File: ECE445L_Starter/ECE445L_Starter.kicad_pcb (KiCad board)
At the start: 2 copper layers, 115 x 94 mm, 20 parts, among them J101 EXT_3V3, Q101 IRLD024PBF, SW101 UP, SW102 DOWN, SW103 LEFT, SW104 RIGHT, SW105 MODE, U101 EK-TM4C123GXL, U102 ESP8266-1, U103 Adafruit ST7735R

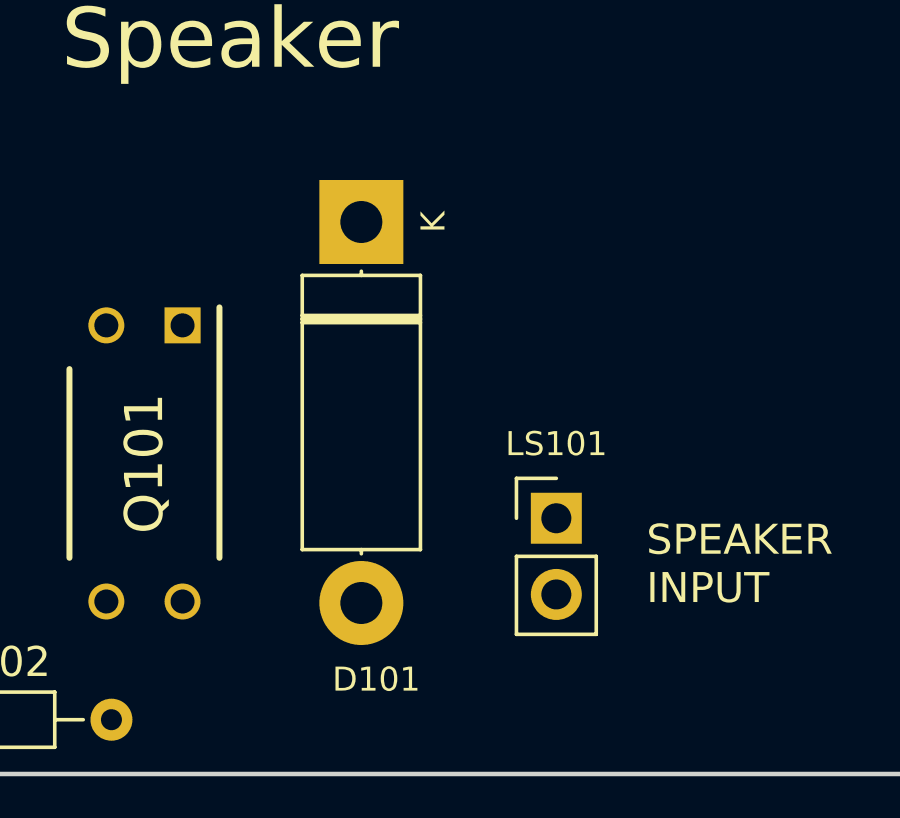
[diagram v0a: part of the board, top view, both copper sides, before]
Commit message: update all symbols and re-sync footprints in the KiCad projects
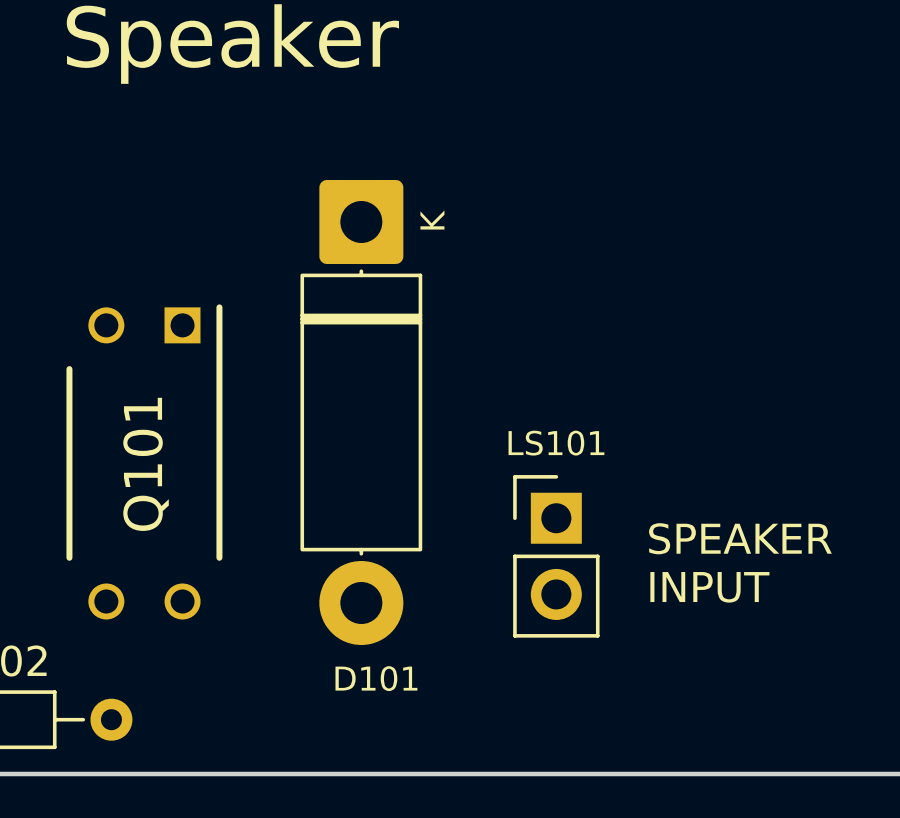
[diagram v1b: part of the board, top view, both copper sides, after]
